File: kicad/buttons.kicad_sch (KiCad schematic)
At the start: 4 parts

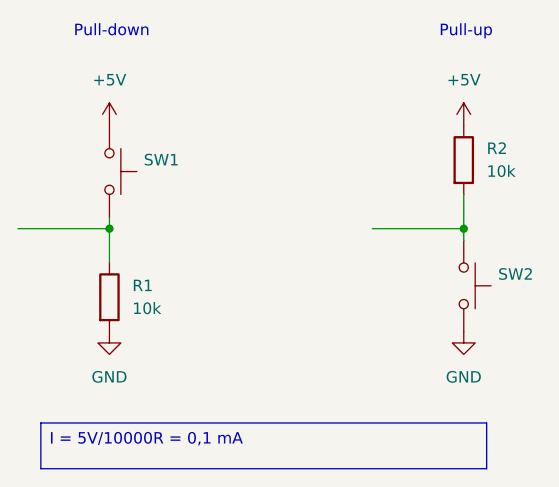
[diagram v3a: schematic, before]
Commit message: terminato collegamento ATMEGA328P
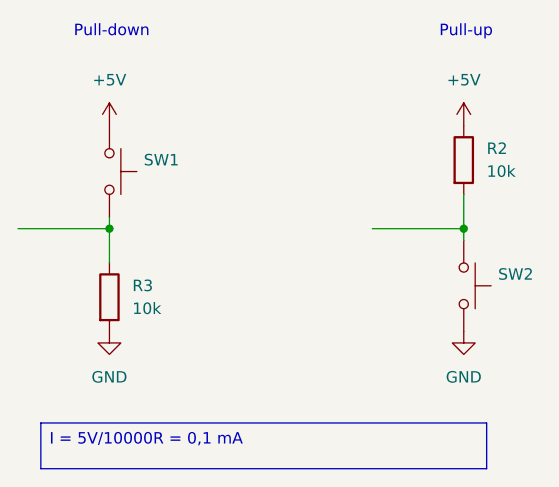
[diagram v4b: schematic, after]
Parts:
- renumbered R1 to R3
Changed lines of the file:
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@@
 		(dnp no)
 		(fields_autoplaced yes)
-		(property "Reference" "#PWR06"
+		(property "Reference" "#PWR019"
 			(at 93.98 41.91 0)
 			(effects
@@
 			(project "electronics-schemas"
 				(path "/f1ade40e-ee4b-4e00-b57d-44850604005b/fed83971-841f-4809-a5b6-eca8a2d26e94"
-					(reference "#PWR06")
+					(reference "#PWR019")
 					(unit 1)
 				)
@@
 		(dnp no)
 		(fields_autoplaced yes)
-		(property "Reference" "#PWR01"
+		(property "Reference" "#PWR020"
 			(at 54.61 67.31 0)
 			(effects
@@
 			(project ""
 				(path "/f1ade40e-ee4b-4e00-b57d-44850604005b/fed83971-841f-4809-a5b6-eca8a2d26e94"
-					(reference "#PWR01")
+					(reference "#PWR020")
 					(unit 1)
 				)
@@
 		(dnp no)
 		(fields_autoplaced yes)
-		(property "Reference" "R1"
+		(property "Reference" "R3"
 			(at 57.15 55.8799 0)
 			(effects
@@
 			(project ""
 				(path "/f1ade40e-ee4b-4e00-b57d-44850604005b/fed83971-841f-4809-a5b6-eca8a2d26e94"
-					(reference "R1")
+					(reference "R3")
 					(unit 1)
 				)
@@
 		(dnp no)
 		(fields_autoplaced yes)
-		(property "Reference" "#PWR07"
+		(property "Reference" "#PWR021"
 			(at 93.98 67.31 0)
 			(effects
@@
 			(project "electronics-schemas"
 				(path "/f1ade40e-ee4b-4e00-b57d-44850604005b/fed83971-841f-4809-a5b6-eca8a2d26e94"
-					(reference "#PWR07")
+					(reference "#PWR021")
 					(unit 1)
 				)
@@
 		(dnp no)
 		(fields_autoplaced yes)
-		(property "Reference" "#PWR05"
+		(property "Reference" "#PWR018"
 			(at 54.61 41.91 0)
 			(effects
@@
 			(project ""
 				(path "/f1ade40e-ee4b-4e00-b57d-44850604005b/fed83971-841f-4809-a5b6-eca8a2d26e94"
-					(reference "#PWR05")
-					(unit 1)
-				)
+					(reference "#PWR018")
+					(unit 1)
+				)
